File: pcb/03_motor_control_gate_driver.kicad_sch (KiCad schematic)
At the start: 2 parts, among them IC1 DRV8323SRTAR, Q1 TPW1R306PL

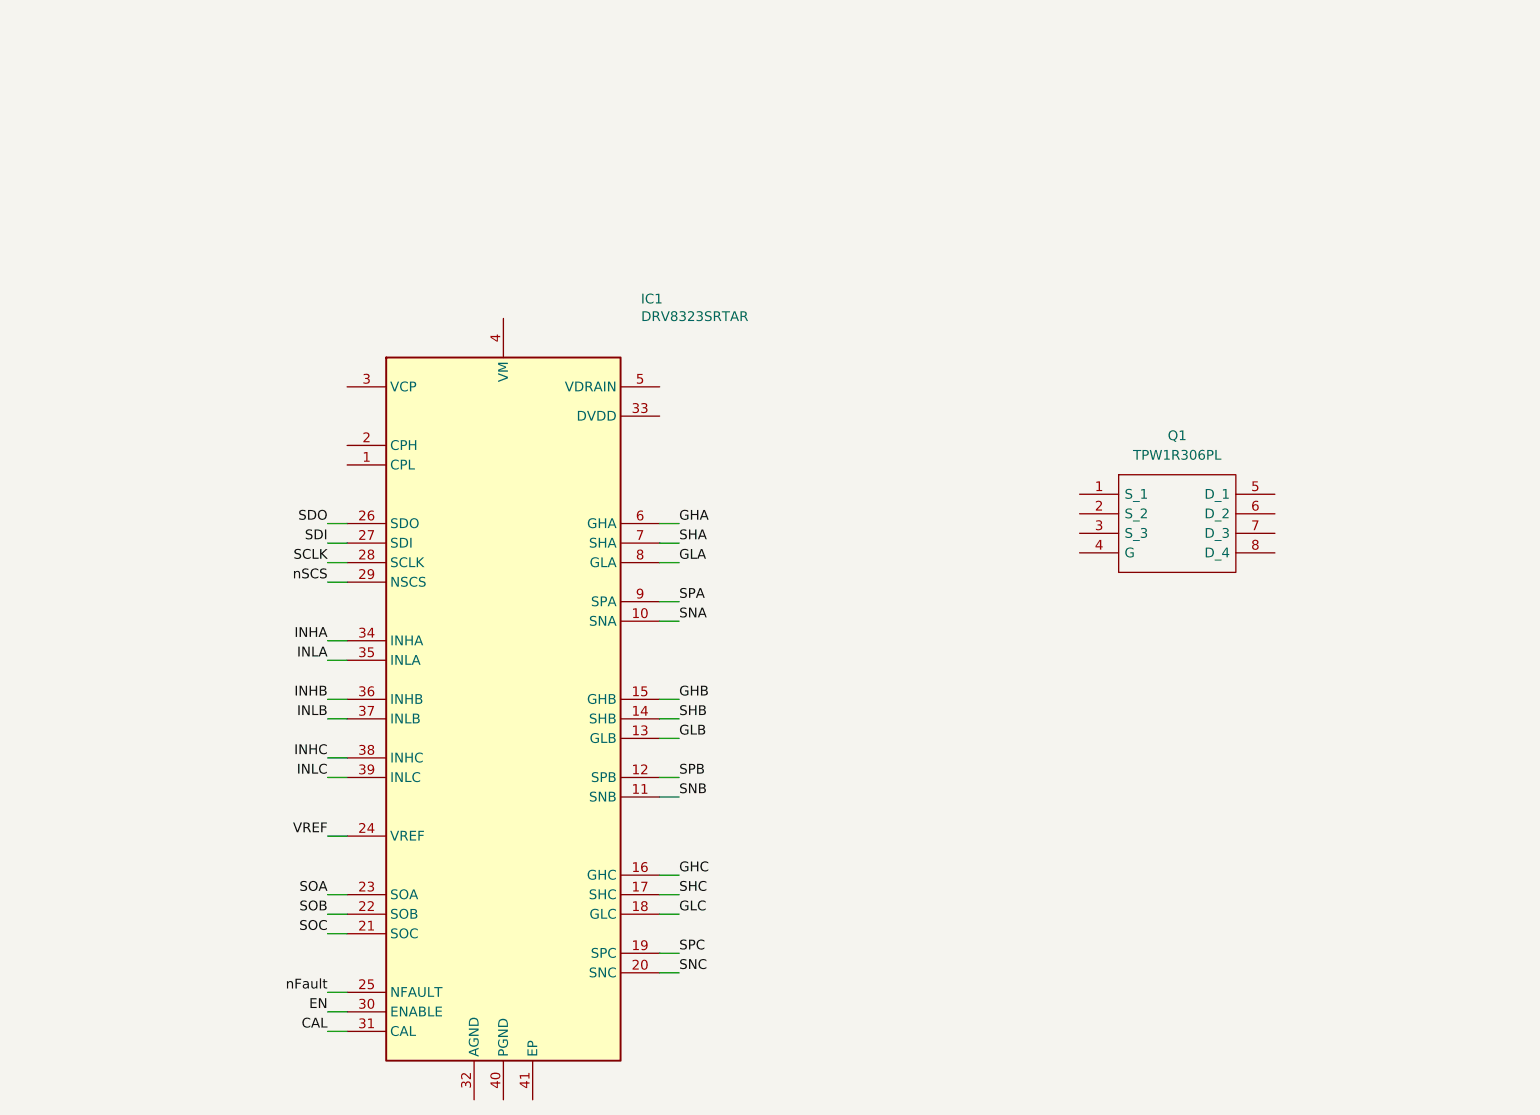
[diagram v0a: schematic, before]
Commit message: Set up gate driver circuitry according to the datasheet
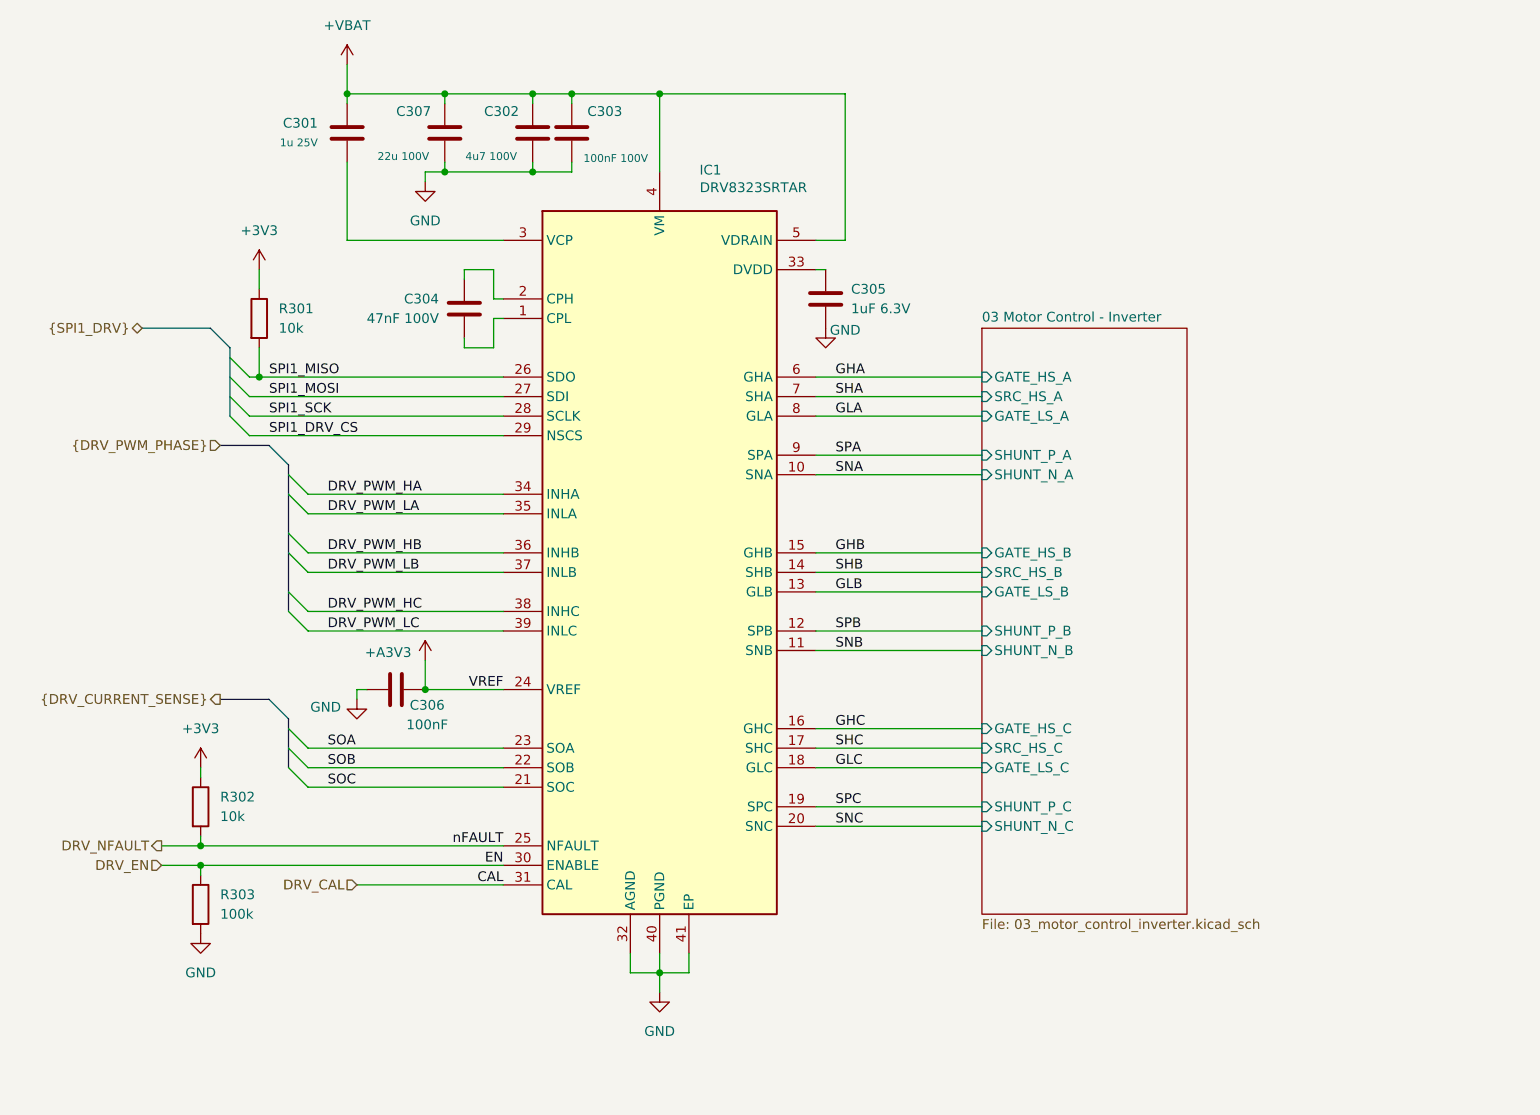
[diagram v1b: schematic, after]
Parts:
- removed Q1: TPW1R306PL, FluxNode-FOC:SOP_ADVANCE, symbol FluxNode-FOC:TPW1R306PL
- added C301: 1u 25V, FluxNode-FOC:C_0603_1608_DensityHigh, symbol Device:C
- added C302: 4u7 100V, FluxNode-FOC:C_1206_3216_DensityHigh, symbol Device:C
- added C303: 100nF 100V, FluxNode-FOC:C_0603_1608_DensityHigh, symbol Device:C
- added C304: 47nF 100V, symbol Device:C
- added C305: 1uF 6.3V, symbol Device:C
- added C306: 100nF, symbol Device:C
- added C307: 22u 100V, symbol Device:C
- added R301, R302: 10k, symbol Device:R
- added R303: 100k, symbol Device:R
- IC1: footprint QFN50P600X600X80-41N-D -> FluxNode-FOC:QFN50P600X600X80-41N-D
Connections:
- net at IC1.1 (CPL): now also C304.2
- net at IC1.2 (CPH): now also C304.1
- net at IC1.3 (VCP): now also C301.2
- net GND: now reaches IC1.32 (AGND)
- net GND: now also IC1.40 (PGND), IC1.41 (EP), C302.2, C303.2, C305.2, C306.2, C307.2, R303.2
- net at IC1.33 (DVDD): now also C305.1
- net +VBAT: now reaches IC1.4 (VM)
- net +VBAT: now also IC1.5 (VDRAIN), C301.1, C302.1, C303.1, C307.1
- net CAL renamed DRV_CAL
- net EN renamed DRV_EN
- net DRV_EN: now also R303.1
- net INHA renamed DRV_PWM_HA
- net INHB renamed DRV_PWM_HB
- net INHC renamed DRV_PWM_HC
- net INLA renamed DRV_PWM_LA
- net INLB renamed DRV_PWM_LB
- net INLC renamed DRV_PWM_LC
- net SCLK renamed SPI1_SCK
- net SDI renamed SPI1_MOSI
- net SDO renamed SPI1_MISO
- net SPI1_MISO: now also R301.2
- net VREF renamed +A3V3
- net +A3V3: now also C306.1
- net nFault renamed DRV_NFAULT
- net DRV_NFAULT: now also R302.2
- net nSCS renamed SPI1_DRV_CS
- new net +3V3: R301.1, R302.1
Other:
- added sheet 03 Motor Control - Inverter (03_motor_control_inverter.kicad_sch)
- moved on the sheet: IC1

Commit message: Unified all different LCSC part numbers of the same exact components to just one variant
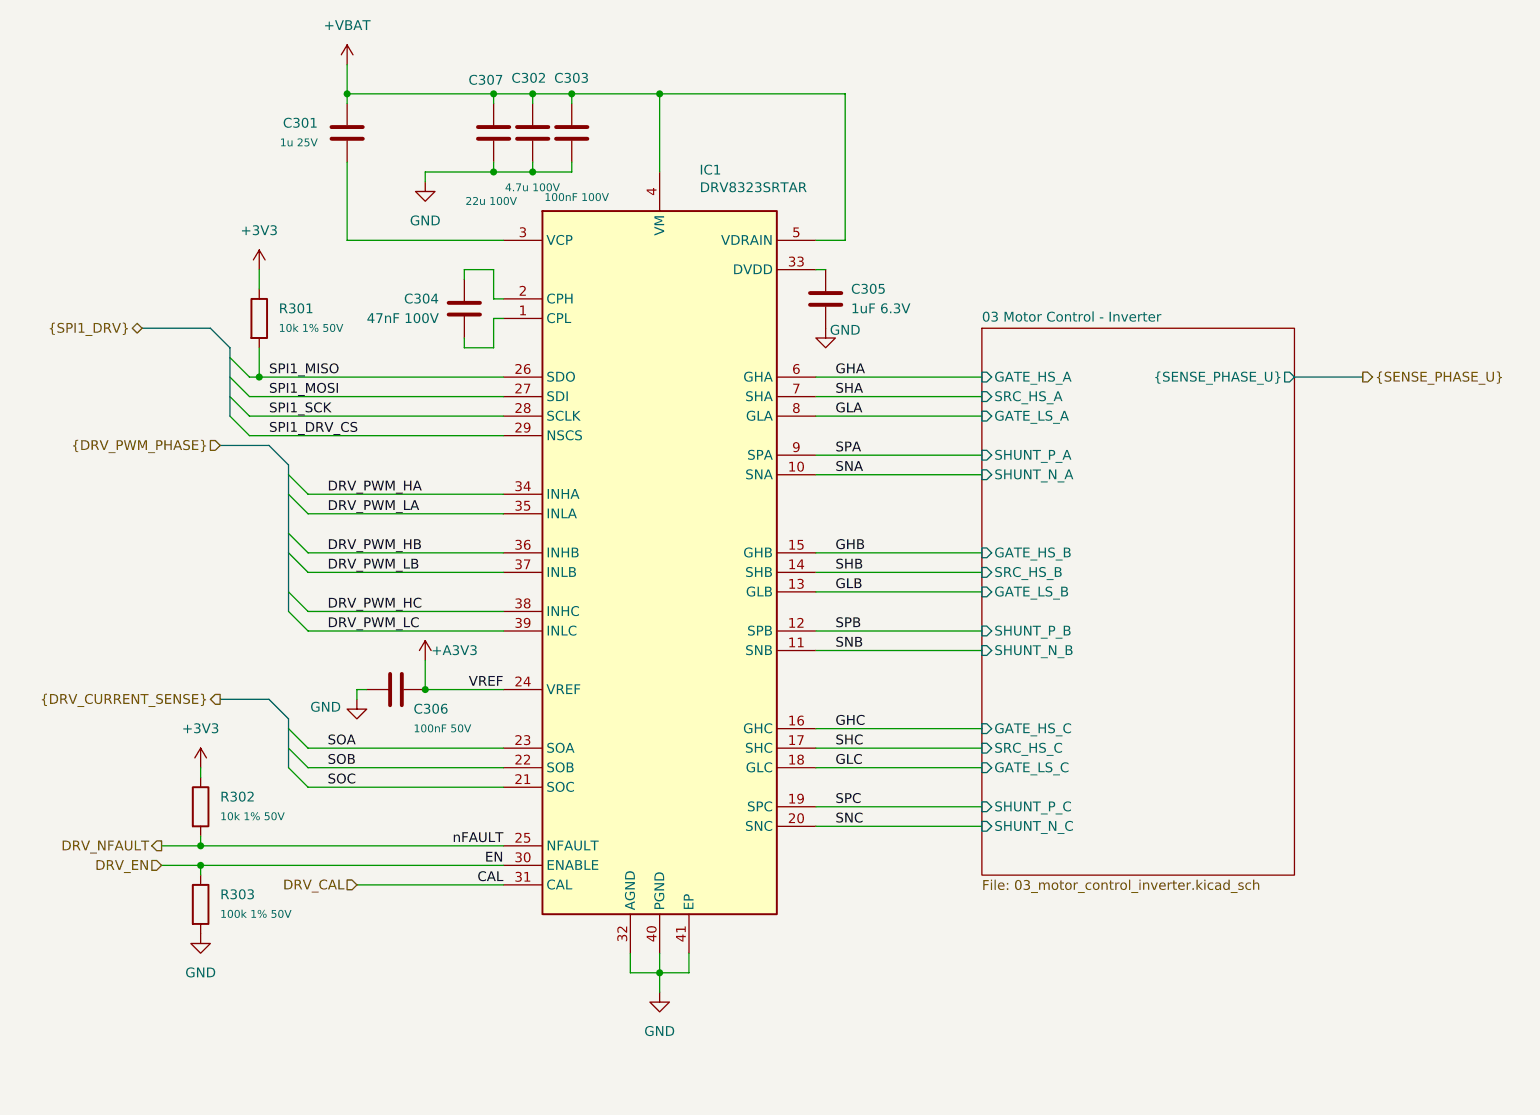
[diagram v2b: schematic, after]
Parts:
- C302: value 4u7 100V -> 4.7u 100V; LCSC C47117455 -> C33546020; MPN CIA1206X7R475K101NT -> HHV1206R7475M101NSPJ
- C304: footprint (none) -> FluxNode-FOC:C_0603_1608_DensityHigh; LCSC (none) -> C5360857; MPN (none) -> TCC0603X7R473K101CT
- C305: footprint (none) -> FluxNode-FOC:C_0402_1005_DensityHigh; LCSC (none) -> C5189823; MPN (none) -> CS1005X5R105K6R3NR
- C306: value 100nF -> 100nF 50V; footprint (none) -> FluxNode-FOC:C_0402_1005_DensityHigh; LCSC (none) -> C361198; MPN (none) -> C1005X7R1H104KT000F
- C307: footprint (none) -> FluxNode-FOC:C_1210_3225_DensityHigh; LCSC (none) -> C576517; MPN (none) -> GRM32EC72A106KE05L
- R301, R302: value 10k -> 10k 1% 50V; footprint (none) -> FluxNode-FOC:R_0402_1005_DensityHigh; LCSC (none) -> C723366; MPN (none) -> RT0402FRE0710KL
- R303: value 100k -> 100k 1% 50V; footprint (none) -> FluxNode-FOC:R_0402_1005_DensityHigh; LCSC (none) -> C728576; MPN (none) -> RT0402FRE07100KL
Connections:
- net +A3V3: now also C306.2; no longer C306.1
- net GND: now also C306.1; no longer C306.2
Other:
- sheet 03 Motor Control - Inverter ports: added {SENSE_PHASE_U}; removed none
- company: (none) -> PhiMai
- moved on the sheet: C307
